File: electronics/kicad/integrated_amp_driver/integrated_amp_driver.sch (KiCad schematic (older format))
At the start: 38 parts, among them J1 CONN_01, J2 PDSE1, J3 Conn_01x04, P4 CONN_6, P5 CONN_6, U1 LM7805, U14 MCP4725SOT-23, U15 TS912IDT, U16 MCP4725SOT-23, U20 MCP1416T-E_OT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

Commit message: Amp built
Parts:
- removed J1: CONN_01, 1X01, symbol SparkFun-Connectors:CONN_01
- removed U?: Teensy-LC, symbol teensy:Teensy-LC
- added C?: 10uF, 1206, symbol SparkFun-Capacitors:1.0UF-1206-50V-10%
- added C?: 0.1 uF, 0603, symbol SparkFun-Capacitors:0.1UF-0603-25V-5%
- added J? (x2): Conn_01x14_Female, symbol Connector:Conn_01x14_Female
- added P1, P2: CONN_6, Connectors2:1X06-SMD_RA_MALE, symbol conn:CONN_6
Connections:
- net labels added: AMP_DRAIN_SUPPLY, RX0, RX3, TX0, TX3
- wire segments 26 -> 27
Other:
- moved on the sheet: J3, R5, U8

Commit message: Driver
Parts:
- removed P1: CONN_6, Connectors2:1X06-SMD_RA_MALE, symbol conn:CONN_6
- added C10, C6, C8, C9, C?: 0.1 uF, 0603, symbol SparkFun-Capacitors:0.1UF-0603-25V-5%
- added J5: CONN_03, Connectors2:1X03_SMD_RA_MALE, symbol SparkFun-Connectors:CONN_03
- added JP1: Jumper, 0xDBFB7:JUMPER_5104, symbol Device:Jumper
- J1, J4: renamed from J?; footprint (none) -> Connector_PinHeader_2.54mm:PinHeader_1x14_P2.54mm_Vertical_SMD_Pin1Right
- gave numbers to parts that had none: 2
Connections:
- net 12V: now also U4.3 (VI), J5.2
- net 3.3V: now also U4.2 (VO), C?.1
- net 5V: now also C10.1, C6.1, C8.1, C9.1
- net GAIN_DAC_I2C_SELECT: now also J1.3 (Pin_3)
- net GATE_DAC_I2C_SELECT: now also J1.2 (Pin_2)
- net GND: now also U4.1 (GND), C10.2, C6.2, C8.2, C9.2, C?.2, J5.1
- net RX0: now also P2.1
- net RX3: now also P2.4
- net TUNING_DAC_I2C_SELECT: now also J1.1 (Pin_1)
- net TX0: now also P2.2
- net TX3: now also P2.5
- net ~AMP_DRAIN_CONTROL: now also J1.8 (Pin_8)
- net ~VCO_POWER_CONTROL: now also J1.7 (Pin_7)
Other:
- moved on the sheet: J3, J4, P2, U4

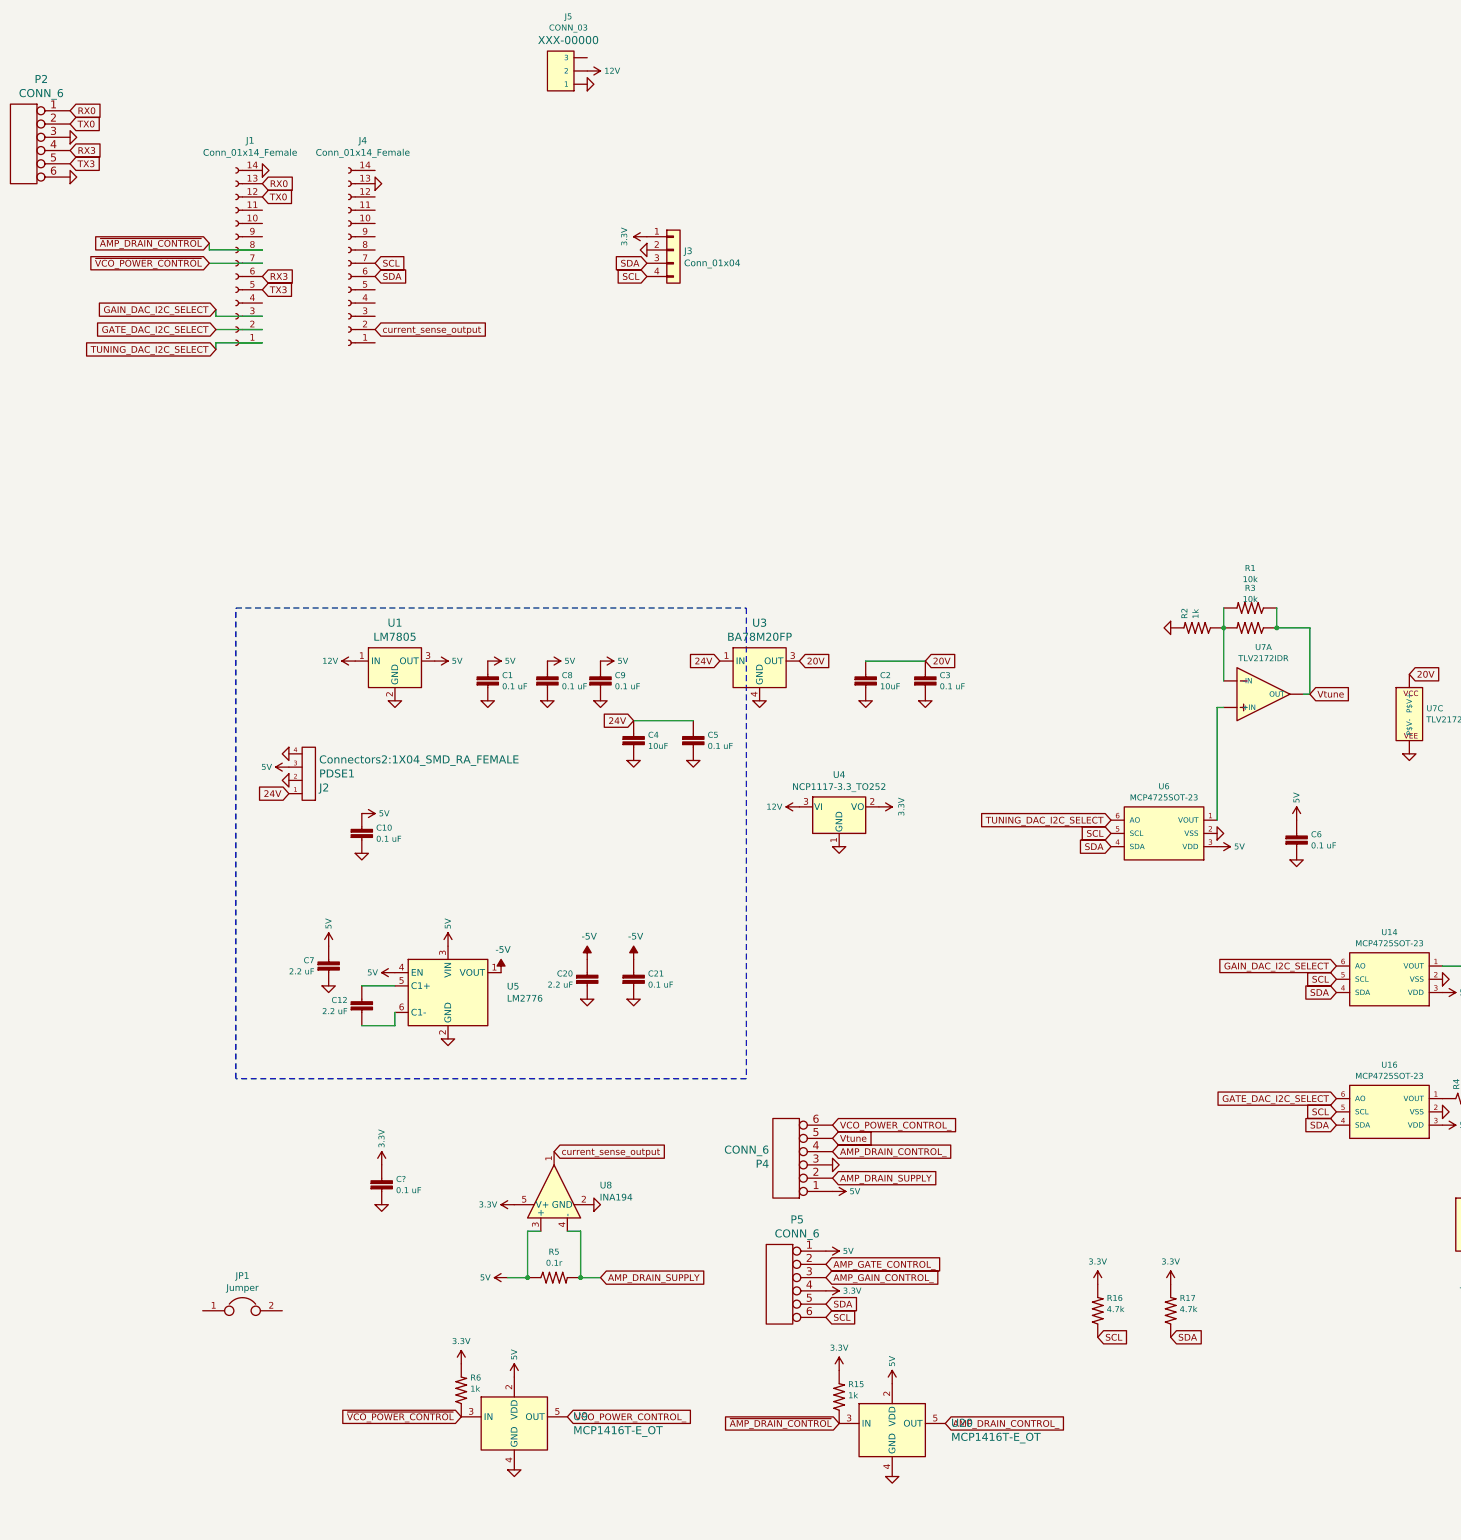
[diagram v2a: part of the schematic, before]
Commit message: Too many vias
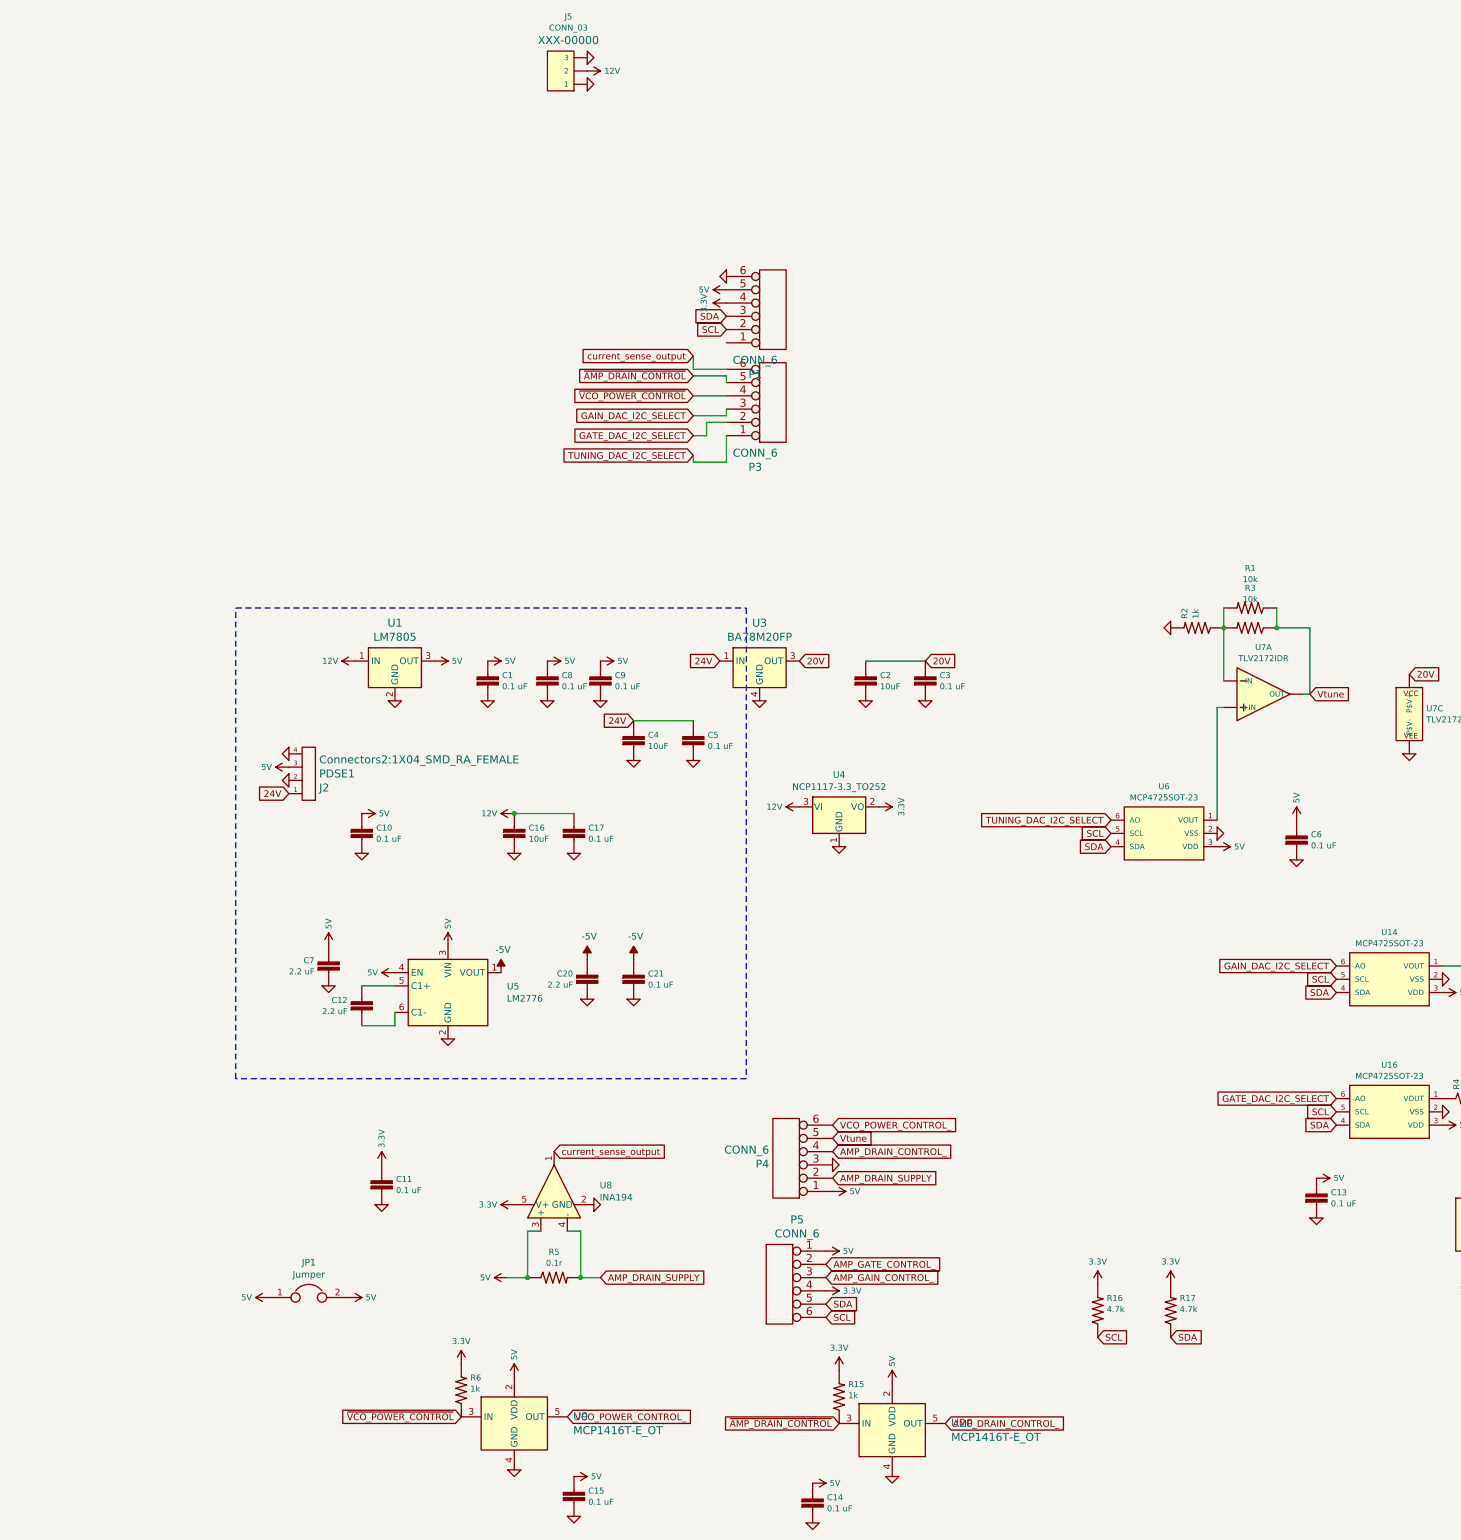
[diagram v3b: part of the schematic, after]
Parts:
- removed J1, J4: Conn_01x14_Female, Connector_PinHeader_2.54mm:PinHeader_1x14_P2.54mm_Vertical_SMD_Pin1Right, symbol Connector:Conn_01x14_Female
- removed J3: Conn_01x04, Connector_PinHeader_2.54mm:PinHeader_1x04_P2.54mm_Vertical_SMD_Pin1Left, symbol Connector_Generic:Conn_01x04
- removed P2: CONN_6, Connectors2:1X06-SMD_RA_MALE, symbol conn:CONN_6
- added C13, C14, C15, C17: 0.1 uF, 0603, symbol SparkFun-Capacitors:0.1UF-0603-25V-5%
- added C16: 10uF, 1206, symbol SparkFun-Capacitors:1.0UF-1206-50V-10%
- added P1, P3: CONN_6, Connectors2:1X06-SMD_RA_MALE, symbol conn:CONN_6
- JP1: footprint 0xDBFB7:JUMPER_5104 -> 0xDBFB7:JUMPER_5102
- gave numbers to parts that had none: 1
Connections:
- net 12V: now also C16.1, C17.1
- net 3.3V: now also P1.4
- net 5V: now also JP1.1, JP1.2, C13.1, C14.1, C15.1, P1.5
- net GAIN_DAC_I2C_SELECT: now also P3.3
- net GATE_DAC_I2C_SELECT: now also P3.2
- net GND: now also J5.3, C13.2, C14.2, C15.2, C16.2, C17.2, P1.6
- net SCL: now also P1.2
- net SDA: now also P1.3
- net TUNING_DAC_I2C_SELECT: now also P3.1
- net current_sense_output: now also P3.6
- net ~AMP_DRAIN_CONTROL: now also P3.5
- net ~VCO_POWER_CONTROL: now also P3.4
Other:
- moved on the sheet: JP1

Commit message: this driver is being a right bastard
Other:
- moved on the sheet: C6, J2, R1, R2, R3, U6, U7A, U7C
